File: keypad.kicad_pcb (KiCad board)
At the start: 2 copper layers, 101.6 x 38.1 mm, 27 parts, among them SW1 SW_Push, U1 ATmega32U4-AU, Y1 16MHz

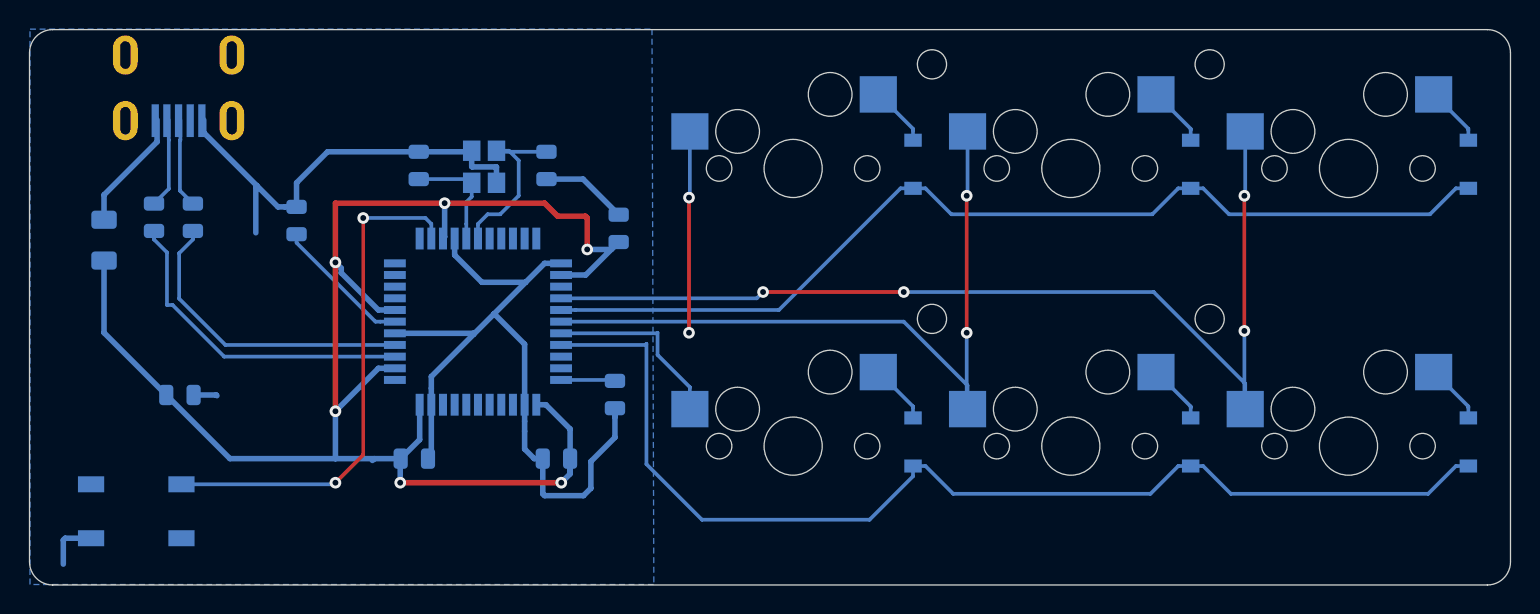
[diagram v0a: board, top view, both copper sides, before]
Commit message: screws redone, switch moved
e
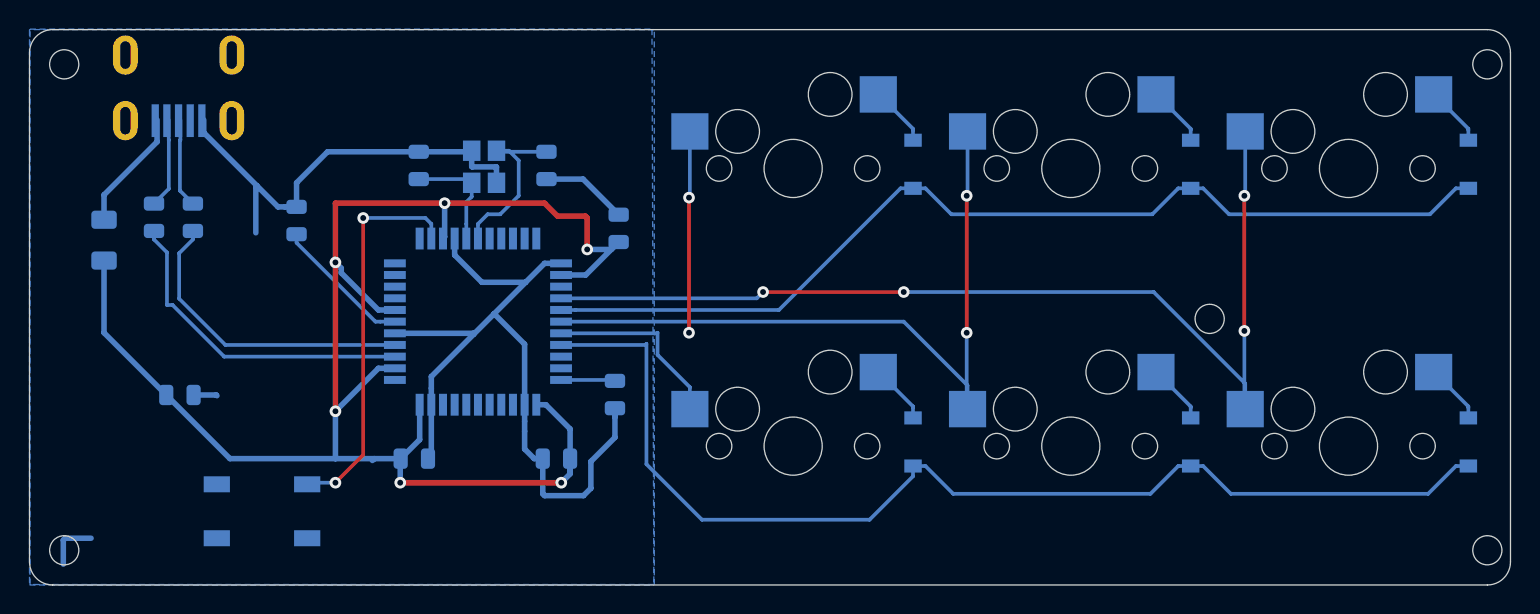
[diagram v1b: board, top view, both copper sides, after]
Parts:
- moved SW1 8.63 mm to (170.7, 135.4)
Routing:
- net Net-(SW1-Pad2): track 35.4 -> 26.9 mm
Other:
- outline, holes or cut-outs redrawn
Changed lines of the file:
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@@
   (general
     (thickness 1.6)
-    (drawings 22)
-    (tracks 243)
+    (drawings 23)
+    (tracks 244)
     (zones 0)
     (modules 27)
@@
   )
   (module random-keyboard-parts:SKQG-1155865 (layer B.Cu)
-    (at 162.104 135.437 180)
+    (at 170.73125 135.437 180)
     (attr smd)
     (fp_text reference SW1 (at 0 -4.064) (layer B.SilkS)
@@
     )
   )
+  (gr_circle (center 254.79375 138.1125) (end 255.79375 138.13155) (layer Edge.Cuts) (width 0.05))
+  (gr_circle (center 254.79375 104.775) (end 255.79375 104.79405) (layer Edge.Cuts) (width 0.05))
+  (gr_circle (center 157.1625 138.1125) (end 158.1625 138.13155) (layer Edge.Cuts) (width 0.05))
+  (gr_circle (center 157.1625 104.775) (end 158.1625 104.79405) (layer Edge.Cuts) (width 0.05))
   (dimension 5.2 (width 0.15) (layer Dwgs.User)
     (gr_text "5.200 mm" (at 155.8625 135.437 270) (layer Dwgs.User)
@@
     (arrow2b (pts (xy 154.78125 108.74375) (xy 155.907754 108.157329)))
   )
-  (gr_circle (center 235.74375 104.775) (end 236.74375 104.79405) (layer Edge.Cuts) (width 0.05))
-  (gr_circle (center 216.69375 104.775) (end 217.69375 104.79405) (layer Edge.Cuts) (width 0.05))
   (gr_circle (center 235.74375 122.2375) (end 236.74375 122.25655) (layer Edge.Cuts) (width 0.05))
-  (gr_circle (center 216.69375 122.2375) (end 217.69375 122.25655) (layer Edge.Cuts) (width 0.05))
   (gr_line (start 154.78125 138.90625) (end 154.78125 103.98125) (layer Edge.Cuts) (width 0.05))
   (gr_line (start 254.79375 140.49375) (end 156.36875 140.49375) (layer Edge.Cuts) (width 0.05))
@@
   (segment (start 191.247 126.428) (end 194.881 126.428) (width 0.254) (layer B.Cu) (net 22))
   (via (at 175.768 133.477) (size 0.8) (drill 0.4) (layers F.Cu B.Cu) (net 23))
-  (segment (start 165.204 133.587) (end 175.658 133.587) (width 0.254) (layer B.Cu) (net 23))
   (segment (start 175.658 133.587) (end 175.768 133.477) (width 0.254) (layer B.Cu) (net 23))
   (via (at 177.673 115.316) (size 0.8) (drill 0.4) (layers F.Cu B.Cu) (net 23))
@@
   (segment (start 181.939 115.316) (end 182.347 115.724) (width 0.254) (layer B.Cu) (net 23))
   (segment (start 177.673 115.316) (end 181.939 115.316) (width 0.254) (layer B.Cu) (net 23))
+  (segment (start 173.94125 133.477) (end 173.83125 133.587) (width 0.254) (layer B.Cu) (net 23))
+  (segment (start 175.768 133.477) (end 173.94125 133.477) (width 0.254) (layer B.Cu) (net 23))
   (zone (net 1) (net_name GND) (layer B.Cu) (hatch edge 0.508)
     (connect_pads (clearance 0.508))
@@
       )
     )
+  )
+  (zone (net 1) (net_name GND) (layer B.Cu) (hatch edge 0.508)
+    (connect_pads (clearance 0.508))
+    (min_thickness 0.254)
+    (fill yes (arc_segments 32) (thermal_gap 0.508) (thermal_bridge_width 0.508))
+    (polygon
+      (pts
+        (xy 154.78125 140.49375) (xy 197.64375 140.49375) (xy 197.64375 102.39375) (xy 154.78125 102.39375)
+      )
+    )

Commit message: gerber + hole changes
e
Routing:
- net GND: track 97.1 -> 93.5 mm
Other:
- outline, holes or cut-outs redrawn
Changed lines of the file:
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@@
   (general
     (thickness 1.6)
-    (drawings 23)
-    (tracks 244)
+    (drawings 21)
+    (tracks 241)
     (zones 0)
     (modules 27)
@@
   (gr_circle (center 254.79375 138.1125) (end 255.79375 138.13155) (layer Edge.Cuts) (width 0.05))
   (gr_circle (center 254.79375 104.775) (end 255.79375 104.79405) (layer Edge.Cuts) (width 0.05))
-  (gr_circle (center 157.1625 138.1125) (end 158.1625 138.13155) (layer Edge.Cuts) (width 0.05))
-  (gr_circle (center 157.1625 104.775) (end 158.1625 104.79405) (layer Edge.Cuts) (width 0.05))
-  (dimension 5.2 (width 0.15) (layer Dwgs.User)
-    (gr_text "5.200 mm" (at 155.8625 135.437 270) (layer Dwgs.User)
-      (effects (font (size 1 1) (thickness 0.15)))
-    )
-    (feature1 (pts (xy 159.504 138.037) (xy 156.576079 138.037)))
-    (feature2 (pts (xy 159.504 132.837) (xy 156.576079 132.837)))
-    (crossbar (pts (xy 157.1625 132.837) (xy 157.1625 138.037)))
-    (arrow1a (pts (xy 157.1625 138.037) (xy 156.576079 136.910496)))
-    (arrow1b (pts (xy 157.1625 138.037) (xy 157.748921 136.910496)))
-    (arrow2a (pts (xy 157.1625 132.837) (xy 156.576079 133.963504)))
-    (arrow2b (pts (xy 157.1625 132.837) (xy 157.748921 133.963504)))
-  )
-  (dimension 5.2 (width 0.15) (layer Dwgs.User)
-    (gr_text "5.200 mm" (at 162.104 129.66875) (layer Dwgs.User)
-      (effects (font (size 1 1) (thickness 0.15)))
-    )
-    (feature1 (pts (xy 164.704 132.837) (xy 164.704 130.382329)))
-    (feature2 (pts (xy 159.504 132.837) (xy 159.504 130.382329)))
-    (crossbar (pts (xy 159.504 130.96875) (xy 164.704 130.96875)))
-    (arrow1a (pts (xy 164.704 130.96875) (xy 163.577496 131.555171)))
-    (arrow1b (pts (xy 164.704 130.96875) (xy 163.577496 130.382329)))
-    (arrow2a (pts (xy 159.504 130.96875) (xy 160.630504 131.555171)))
-    (arrow2b (pts (xy 159.504 130.96875) (xy 160.630504 130.382329)))
-  )
+  (gr_circle (center 157.95625 138.1125) (end 158.95625 138.13155) (layer Edge.Cuts) (width 0.05))
+  (gr_circle (center 157.95625 104.775) (end 158.95625 104.79405) (layer Edge.Cuts) (width 0.05))
   (dimension 7.941836 (width 0.15) (layer Dwgs.User)
     (gr_text "7.942 mm" (at 149.465812 106.227929 89.30379089) (layer Dwgs.User)
@@
   (segment (start 166.733 109.46) (end 170.3685 113.0955) (width 0.381) (layer B.Cu) (net 1))
   (segment (start 170.3685 113.0955) (end 171.827 114.554) (width 0.381) (layer B.Cu) (net 1))
-  (segment (start 157.099 139.065) (end 157.099 137.414) (width 0.381) (layer B.Cu) (net 1))
-  (segment (start 157.226 137.287) (end 159.004 137.287) (width 0.381) (layer B.Cu) (net 1))
-  (segment (start 157.099 137.414) (end 157.226 137.287) (width 0.381) (layer B.Cu) (net 1))
   (segment (start 194.945 130.369672) (end 193.294 132.020672) (width 0.381) (layer B.Cu) (net 1))
   (segment (start 194.945 128.367) (end 194.945 130.369672) (width 0.381) (layer B.Cu) (net 1))

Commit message: gerbers and measurements
a
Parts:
- moved USB1 3.27 mm to (168.3, 104.2)
- moved R1 3.18 mm to (166.5, 115.3)
- moved R2 3.17 mm to (169.2, 115.3)
- moved F1 1.59 mm to (161.5, 116.8)
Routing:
- net GND: track 93.5 -> 84.2 mm
- net Net-(R2-Pad1): track 21.2 -> 14.3 mm
- net Net-(R1-Pad1): track 22.6 -> 17.3 mm
- net COL0: track 26.6 -> 28.8 mm
- net +5V: track 112.0 -> 111.4 mm
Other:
- board size 101.6 x 38.1 mm -> 99.2 x 38.1 mm
